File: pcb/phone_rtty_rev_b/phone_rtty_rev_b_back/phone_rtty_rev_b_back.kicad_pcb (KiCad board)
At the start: 2 copper layers, 58 x 24 mm, 3 parts

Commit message: Minor changes.
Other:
- outline, holes or cut-outs redrawn
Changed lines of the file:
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@@
     (links 0)
     (no_connects 0)
-    (area 99.924999 99.924999 158.075001 124.075001)
+    (area 78.816667 85.65 164.986666 141.700001)
     (thickness 1.6)
     (drawings 49)
@@
   (gr_line (start 110.4 112.8) (end 116.6 112.8) (angle 90) (layer Dwgs.User) (width 0.05))
   (gr_line (start 113.5 109.7) (end 113.5 115.9) (angle 90) (layer Dwgs.User) (width 0.05))
-  (gr_line (start 125.7 110.4) (end 125.7 117.2) (angle 90) (layer Dwgs.User) (width 0.05))
-  (gr_line (start 121.8 113.8) (end 129.6 113.8) (angle 90) (layer Dwgs.User) (width 0.05))
+  (gr_line (start 125.7 110.8) (end 125.7 117.6) (angle 90) (layer Dwgs.User) (width 0.05))
+  (gr_line (start 121.8 114.2) (end 129.6 114.2) (angle 90) (layer Dwgs.User) (width 0.05))
   (gr_text "PCB level" (at 105 116) (layer Cmts.User)
     (effects (font (size 1.2 1.2) (thickness 0.1)))
@@
     (effects (font (size 1.5 1.5) (thickness 0.3)))
   )
-  (gr_circle (center 125.7 113.8) (end 128.6 113.7) (layer Edge.Cuts) (width 0.15))
+  (gr_circle (center 125.7 114.2) (end 128.6 114.1) (layer Edge.Cuts) (width 0.15))
   (gr_line (start 100 116.7) (end 158 116.7) (angle 90) (layer Dwgs.User) (width 0.05))
   (gr_arc (start 101 101) (end 100 101) (angle 90) (layer Edge.Cuts) (width 0.15))

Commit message: Minor changes to revision B and gerbers.
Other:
- board text added: "RTTY Interface Rev. B Back Panel"
- board text removed: "RTTY Interface Revision B Back Panel"
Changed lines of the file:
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@@
     (links 0)
     (no_connects 0)
-    (area 78.816667 85.65 164.986666 141.700001)
+    (area 78.816667 88.8 164.986666 141.700001)
     (thickness 1.6)
     (drawings 49)
@@
     (visible_elements 7FFFFFFF)
     (pcbplotparams
-      (layerselection 0x010f0_80000001)
+      (layerselection 0x010e0_80000001)
       (usegerberextensions true)
       (excludeedgelayer true)
@@
       (drillshape 0)
       (scaleselection 1)
-      (outputdirectory D:/MyProjects/phone_rtty_interface/gerbers))
+      (outputdirectory gerbers))
   )
   (net 0 "")
@@
   (gr_circle (center 125.7 114.2) (end 128.6 114.1) (layer Edge.Cuts) (width 0.15))
   (gr_line (start 100 116.7) (end 158 116.7) (angle 90) (layer Dwgs.User) (width 0.05))
-  (gr_arc (start 101 101) (end 100 101) (angle 90) (layer Edge.Cuts) (width 0.15))
-  (gr_arc (start 101 123) (end 101 124) (angle 90) (layer Edge.Cuts) (width 0.15))
-  (gr_arc (start 157 123) (end 158 123) (angle 90) (layer Edge.Cuts) (width 0.15))
-  (gr_arc (start 157 101) (end 157 100) (angle 90) (layer Edge.Cuts) (width 0.15))
-  (gr_text "RTTY Interface\nRevision B\nBack Panel" (at 129 90.5) (layer Cmts.User)
+  (gr_arc (start 101 101) (end 100 101) (angle 90) (layer Edge.Cuts) (width 0.1))
+  (gr_arc (start 101 123) (end 101 124) (angle 90) (layer Edge.Cuts) (width 0.1))
+  (gr_arc (start 157 123) (end 158 123) (angle 90) (layer Edge.Cuts) (width 0.1))
+  (gr_arc (start 157 101) (end 157 100) (angle 90) (layer Edge.Cuts) (width 0.1))
+  (gr_text "RTTY Interface Rev. B\nBack Panel" (at 129 92) (layer Cmts.User)
     (effects (font (size 2 2) (thickness 0.3)))
   )
@@
     (effects (font (size 1.5 1.5) (thickness 0.25)))
   )
-  (gr_line (start 158 101) (end 158 123) (angle 90) (layer Edge.Cuts) (width 0.15))
-  (gr_line (start 100 101) (end 100 123) (angle 90) (layer Edge.Cuts) (width 0.15))
-  (gr_line (start 101 100) (end 157 100) (angle 90) (layer Edge.Cuts) (width 0.15))
-  (gr_line (start 101 124) (end 157 124) (angle 90) (layer Edge.Cuts) (width 0.15))
+  (gr_line (start 158 101) (end 158 123) (angle 90) (layer Edge.Cuts) (width 0.1))
+  (gr_line (start 100 101) (end 100 123) (angle 90) (layer Edge.Cuts) (width 0.1))
+  (gr_line (start 101 100) (end 157 100) (angle 90) (layer Edge.Cuts) (width 0.1))
+  (gr_line (start 101 124) (end 157 124) (angle 90) (layer Edge.Cuts) (width 0.1))
   (segment (start 133.5 105) (end 133.7 105.2) (width 0.25) (layer F.Cu) (net 0))
   (segment (start 133.7 105.2) (end 134.5 106) (width 0.25) (layer F.Cu) (net 0))

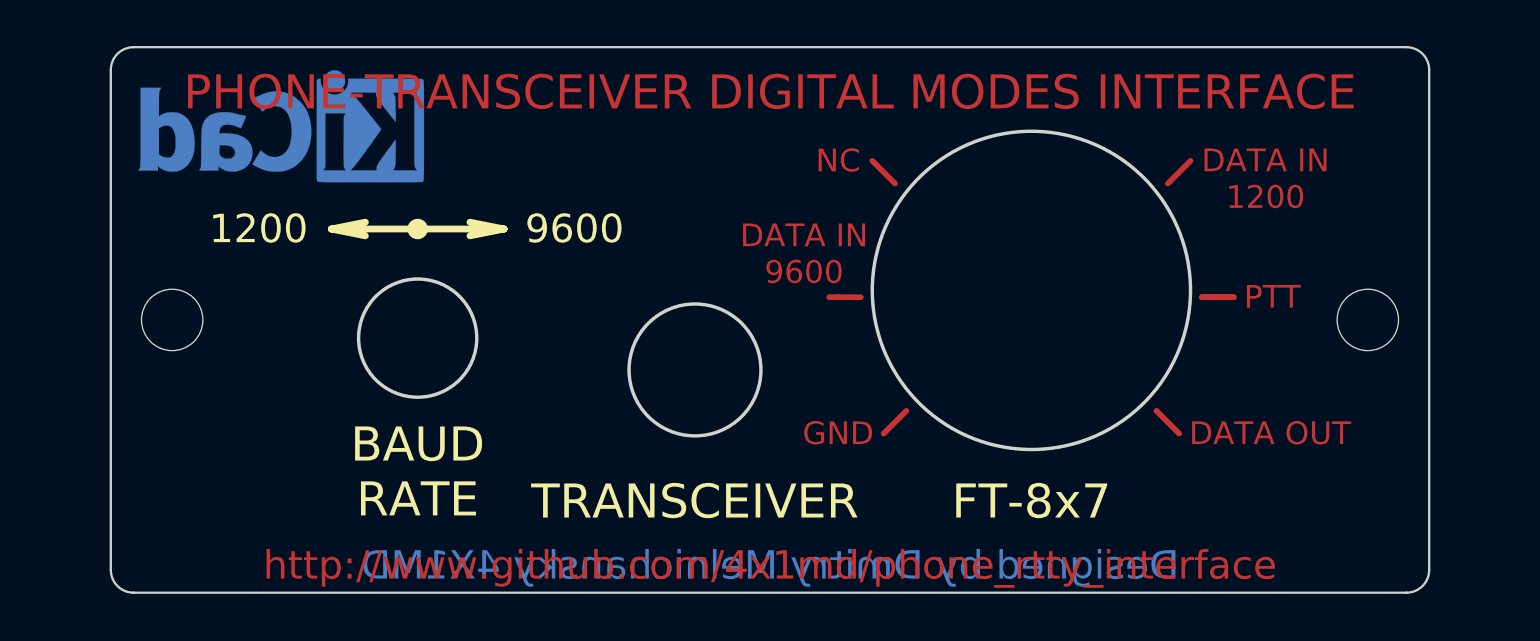
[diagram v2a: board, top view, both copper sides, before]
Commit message: Main board and panels corrections.
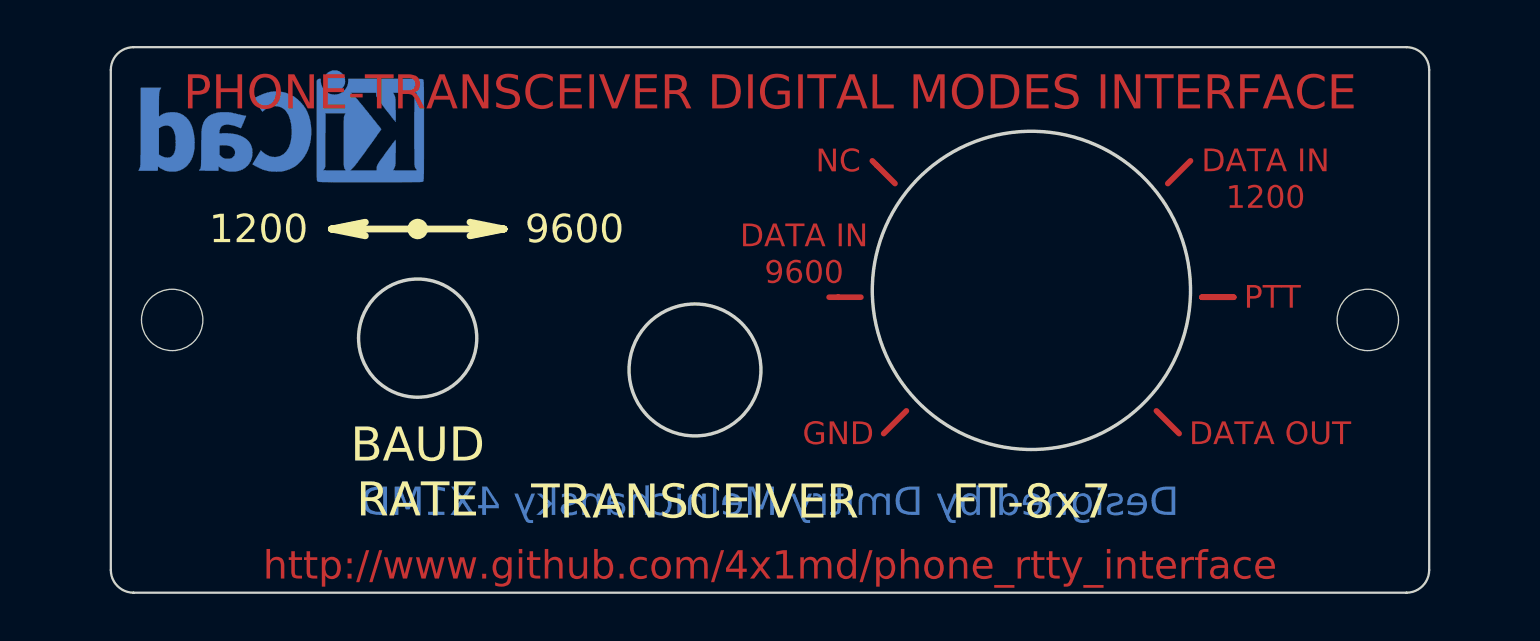
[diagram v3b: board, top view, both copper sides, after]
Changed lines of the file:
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@@
     (effects (font (size 2 2) (thickness 0.3)))
   )
-  (gr_text "Designed by Dmitry Melnichansky 4X1MD" (at 129 122.8) (layer B.Cu)
+  (gr_text "Designed by Dmitry Melnichansky 4X1MD" (at 129 120) (layer B.Cu)
     (effects (font (size 1.25 1.25) (thickness 0.2)) (justify mirror))
   )
